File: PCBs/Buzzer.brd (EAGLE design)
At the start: 13 x 36.4 mm, 3 parts

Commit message: Updated
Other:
- board size 13 x 36.4 mm -> 14.5 x 36.3 mm
- board text added: "PinwheelRobotics"
- board text added: "care@pinwheel"
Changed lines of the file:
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@@
 <setting verticaltext="up"/>
 </settings>
-<grid distance="0.1" unitdist="mm" unit="mm" style="lines" multiple="1" display="yes" altdistance="0.01" altunitdist="mm" altunit="mm"/>
+<grid distance="0.5" unitdist="mm" unit="mm" style="lines" multiple="1" display="yes" altdistance="0.01" altunitdist="mm" altunit="mm"/>
 <layers>
 <layer number="1" name="Top" color="4" fill="1" visible="yes" active="yes"/>
@@
 <layer number="43" name="vRestrict" color="2" fill="10" visible="yes" active="yes"/>
 <layer number="44" name="Drills" color="7" fill="1" visible="no" active="yes"/>
-<layer number="45" name="Holes" color="7" fill="1" visible="no" active="yes"/>
+<layer number="45" name="Holes" color="7" fill="1" visible="yes" active="yes"/>
 <layer number="46" name="Milling" color="3" fill="1" visible="no" active="yes"/>
 <layer number="47" name="Measures" color="7" fill="1" visible="no" active="yes"/>
@@
 <board>
 <plain>
-<wire x1="8.83" y1="2.1" x2="21.85" y2="2.05" width="0" layer="20"/>
-<wire x1="21.85" y1="2.05" x2="21.85" y2="38.35" width="0" layer="20"/>
-<wire x1="21.85" y1="38.35" x2="8.83" y2="38.4" width="0" layer="20"/>
-<wire x1="8.83" y1="38.4" x2="8.83" y2="2.1" width="0" layer="20"/>
+<wire x1="8" y1="36.9741875" x2="8" y2="3.74459375" width="0" layer="20"/>
+<wire x1="8" y1="3.74459375" x2="9.644584375" y2="2.094328125" width="0" layer="20" curve="89.802427"/>
+<wire x1="9.644584375" y1="2.094328125" x2="20.7962875" y2="2.055875" width="0" layer="20"/>
+<wire x1="20.7962875" y1="2.055875" x2="22.5" y2="3.753725" width="0" layer="20" curve="90.211382"/>
+<wire x1="22.5" y1="3.753725" x2="22.5" y2="36.594515625" width="0" layer="20"/>
+<wire x1="22.5" y1="36.594515625" x2="20.744528125" y2="38.356053125" width="0" layer="20" curve="89.802405"/>
+<wire x1="20.744528125" y1="38.356053125" x2="9.425803125" y2="38.395084375" width="0" layer="20"/>
+<wire x1="9.425803125" y1="38.395084375" x2="8" y2="36.9741875" width="0" layer="20" curve="90.193413"/>
+<hole x="10.02" y="36.44" drill="3"/>
+<hole x="20.51" y="36.47" drill="3"/>
+<hole x="9.88" y="4.07" drill="3"/>
+<hole x="20.41" y="4.06" drill="3"/>
+<text x="21.54" y="28.05" size="1.778" layer="22" rot="MR270">care@pinwheel</text>
+<text x="10.56" y="10.35" size="1.778" layer="21" rot="R90">PinwheelRobotics</text>
 </plain>
 <attributes>

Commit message: New Update
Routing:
- net N$1: track 10.4 -> 7.15 mm
- net N$2: track 11.0 -> 8.21 mm
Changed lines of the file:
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@@
 <drawing>
 <settings>
-<setting alwaysvectorfont="yes"/>
+<setting alwaysvectorfont="no"/>
 <setting verticaltext="up"/>
 </settings>
@@
 <wire x1="20.744528125" y1="38.356053125" x2="9.425803125" y2="38.395084375" width="0" layer="20"/>
 <wire x1="9.425803125" y1="38.395084375" x2="8" y2="36.9741875" width="0" layer="20" curve="90.193413"/>
-<hole x="10.02" y="36.44" drill="3"/>
-<hole x="20.51" y="36.47" drill="3"/>
-<hole x="9.88" y="4.07" drill="3"/>
-<hole x="20.41" y="4.06" drill="3"/>
+<hole x="10" y="36.5" drill="3"/>
+<hole x="20.5" y="36.5" drill="3"/>
+<hole x="10" y="4" drill="3"/>
+<hole x="20.5" y="4" drill="3"/>
 <text x="21.54" y="28.05" size="1.778" layer="22" rot="MR270">care@pinwheel</text>
 <text x="10.56" y="10.35" size="1.778" layer="21" rot="R90">PinwheelRobotics</text>
@@
 <attribute name="VALUE" x="19.15" y="16.51" size="1.27" layer="27" ratio="10" rot="R90"/>
 </element>
-<element name="U$1" library="microbit" package="MICROBIT_PAD" value="MICROBIT_PAD" x="15.34" y="31.28" smashed="yes" rot="R180">
-<attribute name="NAME" x="11.75" y="32.3" size="1.27" layer="21" rot="R90"/>
+<element name="U$1" library="microbit" package="MICROBIT_PAD" value="MICROBIT_PAD" x="15.3" y="31.28" smashed="yes" rot="R180">
+<attribute name="NAME" x="11.71" y="32.3" size="1.27" layer="21" rot="R90"/>
 </element>
-<element name="U$2" library="microbit" package="MICROBIT_PAD" value="MICROBIT_PAD" x="15.34" y="9.12" smashed="yes">
-<attribute name="NAME" x="11.53" y="4.04" size="1.27" layer="21" rot="R90"/>
+<element name="U$2" library="microbit" package="MICROBIT_PAD" value="MICROBIT_PAD" x="15.3" y="9.12" smashed="yes">
+<attribute name="NAME" x="11.49" y="5.54" size="1.27" layer="21" rot="R90"/>
 </element>
 </elements>
@@
 <contactref element="SG1" pad="+"/>
 <contactref element="U$1" pad="PAD"/>
-<wire x1="15.5448" y1="34.4424" x2="15.34" y2="34.2376" width="0.1524" layer="16"/>
-<wire x1="15.34" y1="31.28" x2="15.34" y2="34.2376" width="0.1524" layer="16"/>
-<wire x1="15.34" y1="24.13" x2="15.34" y2="31.28" width="2.54" layer="16"/>
+<wire x1="15.34" y1="24.13" x2="15.3" y2="31.28" width="2.54" layer="16"/>
 </signal>
 <signal name="N$2">
@@
 <contactref element="U$2" pad="PAD"/>
 <wire x1="14.917034375" y1="6.382634375" x2="14.6304" y2="6.096" width="0.1524" layer="16"/>
-<wire x1="14.917034375" y1="6.382634375" x2="15.34" y2="9.12" width="0.1524" layer="16"/>
 <wire x1="15.34" y1="16.51" x2="15.34" y2="9.36" width="2.54" layer="16"/>
 <wire x1="15.34" y1="9.36" x2="15.8" y2="8.9" width="2.54" layer="16"/>
-<wire x1="15.34" y1="9.12" x2="15.8" y2="8.9" width="0" layer="19" extent="16-16"/>
+<wire x1="15.8" y1="8.9" x2="15.3" y2="9.12" width="0" layer="19" extent="16-16"/>
+<wire x1="14.917034375" y1="6.382634375" x2="15.8" y2="8.9" width="0" layer="19" extent="16-16"/>
 </signal>
 </signals>

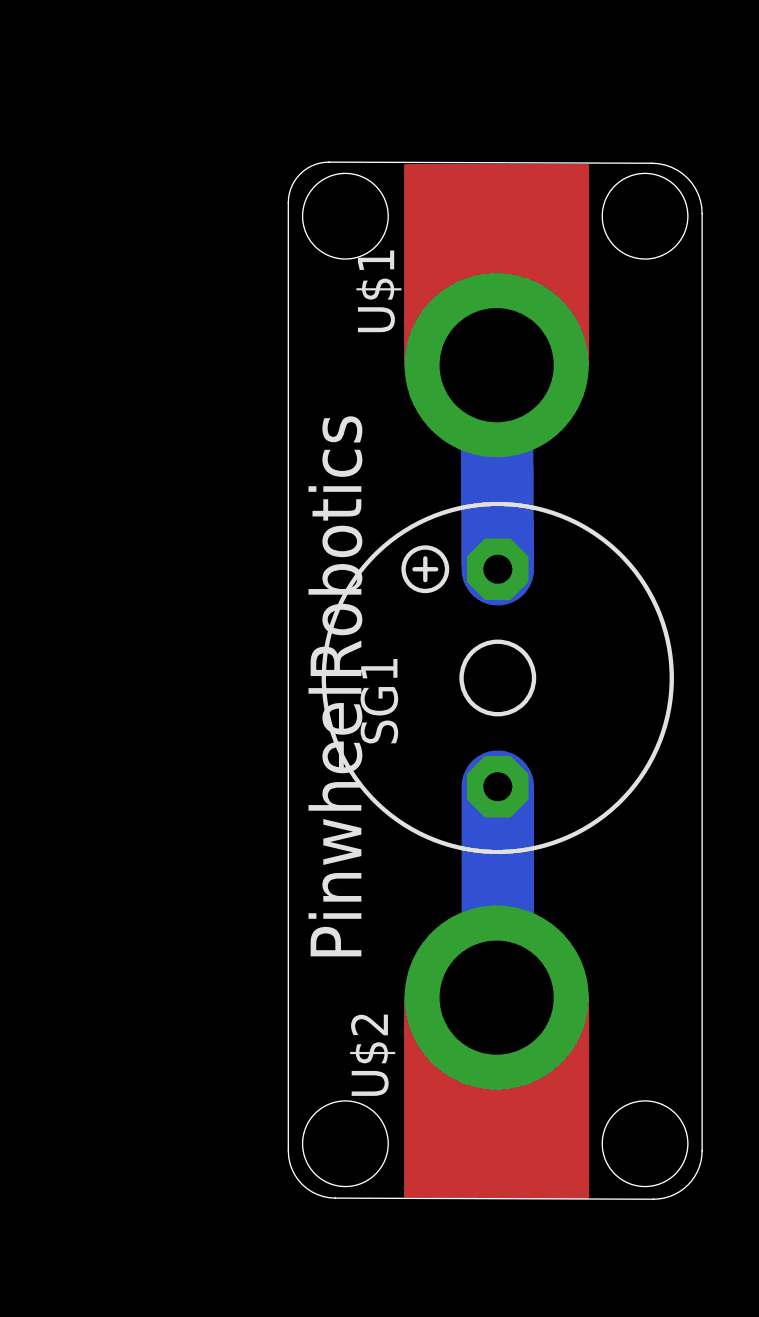
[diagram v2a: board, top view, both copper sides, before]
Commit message: New Update for board curv
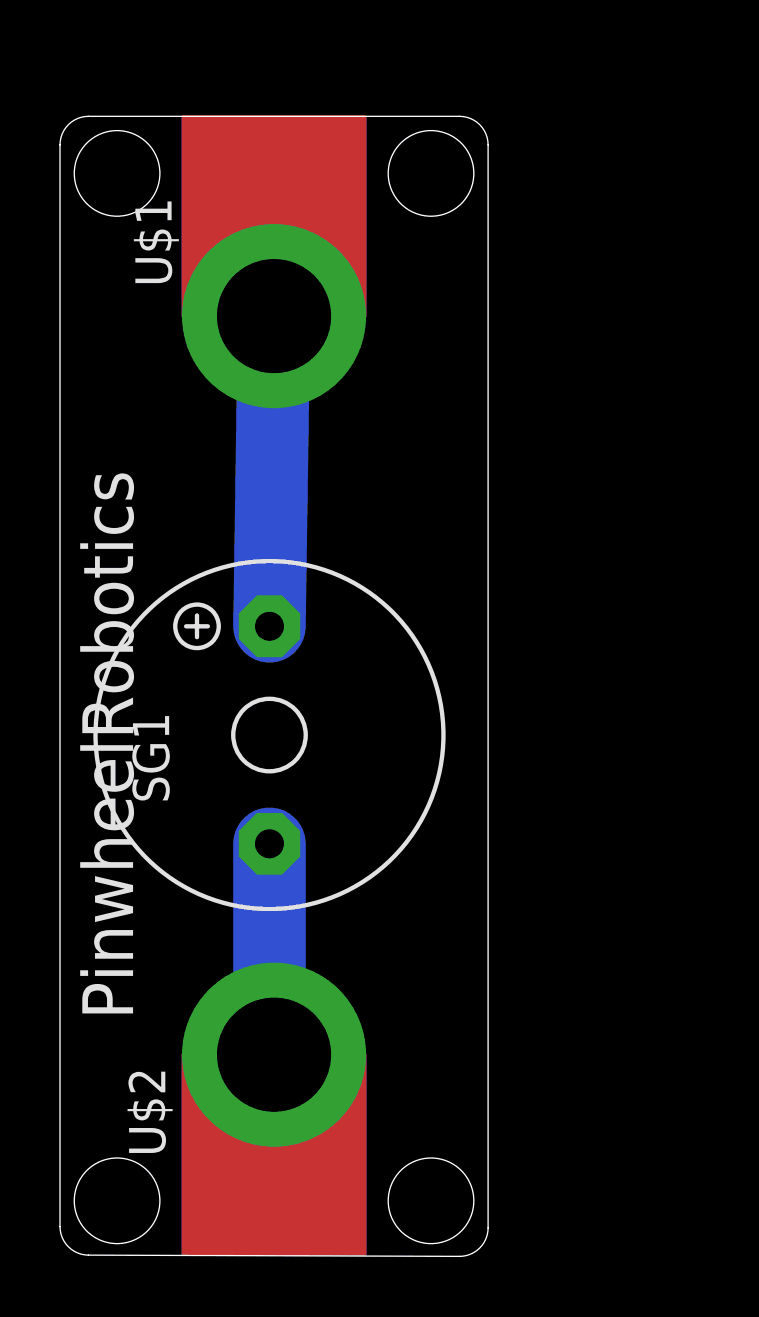
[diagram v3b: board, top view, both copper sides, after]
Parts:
- moved SG1 8.25 mm to (7.34, 18.3)
- moved U$2 8.05 mm to (7.50, 7.12)
- moved U$1 7.99 mm to (7.50, 33.0)
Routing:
- net N$1: track 7.15 -> 10.9 mm
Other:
- board size 14.5 x 36.3 mm -> 15 x 39.9 mm
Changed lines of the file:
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@@
 <drawing>
 <settings>
-<setting alwaysvectorfont="no"/>
+<setting alwaysvectorfont="yes"/>
 <setting verticaltext="up"/>
 </settings>
@@
 <board>
 <plain>
-<wire x1="8" y1="36.9741875" x2="8" y2="3.74459375" width="0" layer="20"/>
-<wire x1="8" y1="3.74459375" x2="9.644584375" y2="2.094328125" width="0" layer="20" curve="89.802427"/>
-<wire x1="9.644584375" y1="2.094328125" x2="20.7962875" y2="2.055875" width="0" layer="20"/>
-<wire x1="20.7962875" y1="2.055875" x2="22.5" y2="3.753725" width="0" layer="20" curve="90.211382"/>
-<wire x1="22.5" y1="3.753725" x2="22.5" y2="36.594515625" width="0" layer="20"/>
-<wire x1="22.5" y1="36.594515625" x2="20.744528125" y2="38.356053125" width="0" layer="20" curve="89.802405"/>
-<wire x1="20.744528125" y1="38.356053125" x2="9.425803125" y2="38.395084375" width="0" layer="20"/>
-<wire x1="9.425803125" y1="38.395084375" x2="8" y2="36.9741875" width="0" layer="20" curve="90.193413"/>
-<hole x="10" y="36.5" drill="3"/>
-<hole x="20.5" y="36.5" drill="3"/>
-<hole x="10" y="4" drill="3"/>
-<hole x="20.5" y="4" drill="3"/>
-<text x="21.54" y="28.05" size="1.778" layer="22" rot="MR270">care@pinwheel</text>
-<text x="10.56" y="10.35" size="1.778" layer="21" rot="R90">PinwheelRobotics</text>
+<wire x1="0.996665625" y1="0.096678125" x2="13.996665625" y2="0.05334375" width="0" layer="20"/>
+<wire x1="13.996665625" y1="0.05334375" x2="15" y2="1.0533375" width="0" layer="20" curve="90.173081"/>
+<wire x1="15" y1="1.0533375" x2="15" y2="39" width="0" layer="20"/>
+<wire x1="15" y1="39" x2="14" y2="40" width="0" layer="20" curve="90"/>
+<wire x1="14" y1="40" x2="1" y2="40" width="0" layer="20"/>
+<wire x1="1" y1="40" x2="0" y2="39" width="0" layer="20" curve="90"/>
+<wire x1="0" y1="39" x2="0" y2="1.096671875" width="0" layer="20"/>
+<wire x1="0" y1="1.096671875" x2="0.996665625" y2="0.096678125" width="0" layer="20" curve="89.808954"/>
+<hole x="2" y="38" drill="3"/>
+<hole x="13" y="38" drill="3"/>
+<hole x="2" y="2" drill="3"/>
+<hole x="13" y="2" drill="3"/>
+<text x="13.54" y="26.05" size="1.778" layer="22" rot="MR270">care@pinwheel</text>
+<text x="2.56" y="8.35" size="1.778" layer="21" rot="R90">PinwheelRobotics</text>
 </plain>
 <attributes>
@@
 </autorouter>
 <elements>
-<element name="SG1" library="buzzer" library_urn="urn:adsk.eagle:library:113" package="F/TMB" package3d_urn="urn:adsk.eagle:package:5260/1" value="F/TMB" x="15.34" y="20.32" smashed="yes" rot="R90">
-<attribute name="MF" value="" x="21.69" y="40.64" size="1.778" layer="27" rot="R90" display="off"/>
-<attribute name="MPN" value="" x="21.69" y="40.64" size="1.778" layer="27" rot="R90" display="off"/>
-<attribute name="NAME" x="11.825" y="17.922" size="1.27" layer="25" ratio="10" rot="R90"/>
-<attribute name="OC_FARNELL" value="unknown" x="21.69" y="40.64" size="1.778" layer="27" rot="R90" display="off"/>
-<attribute name="OC_NEWARK" value="unknown" x="21.69" y="40.64" size="1.778" layer="27" rot="R90" display="off"/>
-<attribute name="POPULARITY" value="1" x="21.69" y="40.64" size="1.778" layer="27" rot="R90" display="off"/>
-<attribute name="VALUE" x="19.15" y="16.51" size="1.27" layer="27" ratio="10" rot="R90"/>
+<element name="SG1" library="buzzer" library_urn="urn:adsk.eagle:library:113" package="F/TMB" package3d_urn="urn:adsk.eagle:package:5260/1" value="F/TMB" x="7.34" y="18.32" smashed="yes" rot="R90">
+<attribute name="MF" value="" x="13.69" y="38.64" size="1.778" layer="27" rot="R90" display="off"/>
+<attribute name="MPN" value="" x="13.69" y="38.64" size="1.778" layer="27" rot="R90" display="off"/>
+<attribute name="NAME" x="3.825" y="15.922" size="1.27" layer="25" ratio="10" rot="R90"/>
+<attribute name="OC_FARNELL" value="unknown" x="13.69" y="38.64" size="1.778" layer="27" rot="R90" display="off"/>
+<attribute name="OC_NEWARK" value="unknown" x="13.69" y="38.64" size="1.778" layer="27" rot="R90" display="off"/>
+<attribute name="POPULARITY" value="1" x="13.69" y="38.64" size="1.778" layer="27" rot="R90" display="off"/>
+<attribute name="VALUE" x="11.15" y="14.51" size="1.27" layer="27" ratio="10" rot="R90"/>
 </element>
-<element name="U$1" library="microbit" package="MICROBIT_PAD" value="MICROBIT_PAD" x="15.3" y="31.28" smashed="yes" rot="R180">
-<attribute name="NAME" x="11.71" y="32.3" size="1.27" layer="21" rot="R90"/>
+<element name="U$1" library="microbit" package="MICROBIT_PAD" value="MICROBIT_PAD" x="7.5" y="33" smashed="yes" rot="R180">
+<attribute name="NAME" x="3.91" y="34.02" size="1.27" layer="21" rot="R90"/>
 </element>
-<element name="U$2" library="microbit" package="MICROBIT_PAD" value="MICROBIT_PAD" x="15.3" y="9.12" smashed="yes">
-<attribute name="NAME" x="11.49" y="5.54" size="1.27" layer="21" rot="R90"/>
+<element name="U$2" library="microbit" package="MICROBIT_PAD" value="MICROBIT_PAD" x="7.5" y="7.12" smashed="yes">
+<attribute name="NAME" x="3.69" y="3.54" size="1.27" layer="21" rot="R90"/>
 </element>
 </elements>
@@
 <contactref element="SG1" pad="+"/>
 <contactref element="U$1" pad="PAD"/>
-<wire x1="15.34" y1="24.13" x2="15.3" y2="31.28" width="2.54" layer="16"/>
+<wire x1="7.34" y1="22.13" x2="7.5" y2="33" width="2.54" layer="16"/>
 </signal>
 <signal name="N$2">
 <contactref element="SG1" pad="-"/>
 <contactref element="U$2" pad="PAD"/>
-<wire x1="14.917034375" y1="6.382634375" x2="14.6304" y2="6.096" width="0.1524" layer="16"/>
-<wire x1="15.34" y1="16.51" x2="15.34" y2="9.36" width="2.54" layer="16"/>
-<wire x1="15.34" y1="9.36" x2="15.8" y2="8.9" width="2.54" layer="16"/>
-<wire x1="15.8" y1="8.9" x2="15.3" y2="9.12" width="0" layer="19" extent="16-16"/>
-<wire x1="14.917034375" y1="6.382634375" x2="15.8" y2="8.9" width="0" layer="19" extent="16-16"/>
+<wire x1="6.917034375" y1="4.382634375" x2="6.6304" y2="4.096" width="0.1524" layer="16"/>
+<wire x1="7.34" y1="14.51" x2="7.34" y2="7.36" width="2.54" layer="16"/>
+<wire x1="7.34" y1="7.36" x2="7.8" y2="6.9" width="2.54" layer="16"/>
+<wire x1="7.8" y1="6.9" x2="7.5" y2="7.12" width="0" layer="19" extent="16-16"/>
+<wire x1="6.917034375" y1="4.382634375" x2="7.8" y2="6.9" width="0" layer="19" extent="16-16"/>
 </signal>
 </signals>
